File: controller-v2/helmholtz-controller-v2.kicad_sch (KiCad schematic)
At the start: 35 parts, among them J1 Screw_Terminal_01x02, J2 Screw_Terminal_01x02, J3 Screw_Terminal_01x02, J4 Screw_Terminal_01x02, U1 BDS63150AFM, U2 BDS63150AFM, U3 INA226, U4 INA226, U5 BDS63150AFM, U6 INA226, U7 RPi_Pico

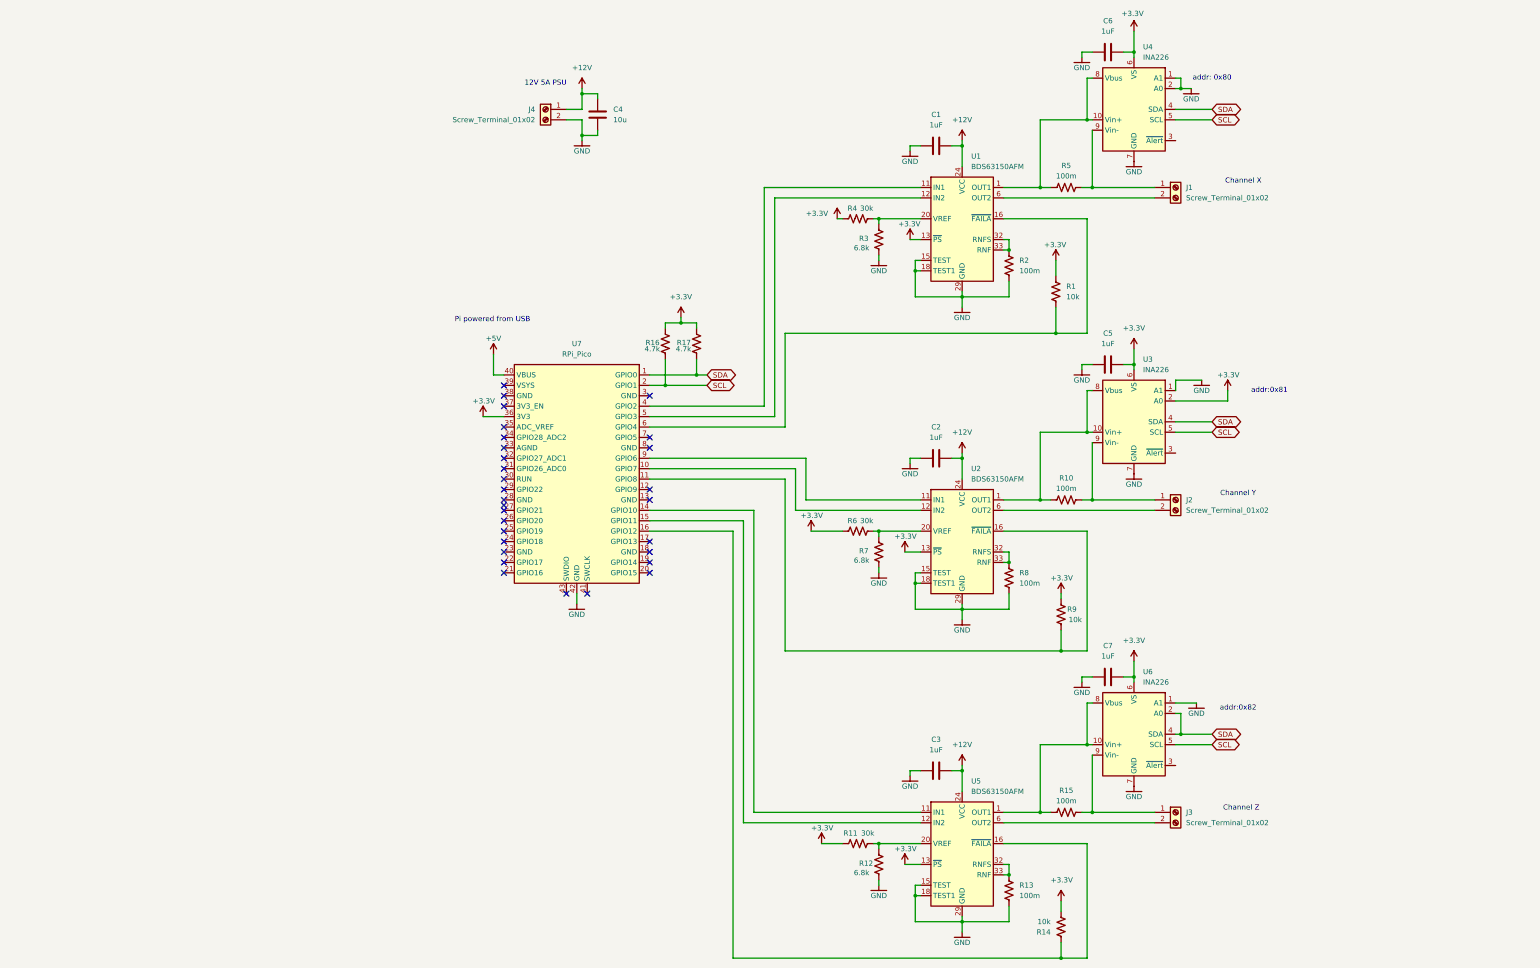
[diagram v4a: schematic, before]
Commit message: Indicators & test points added
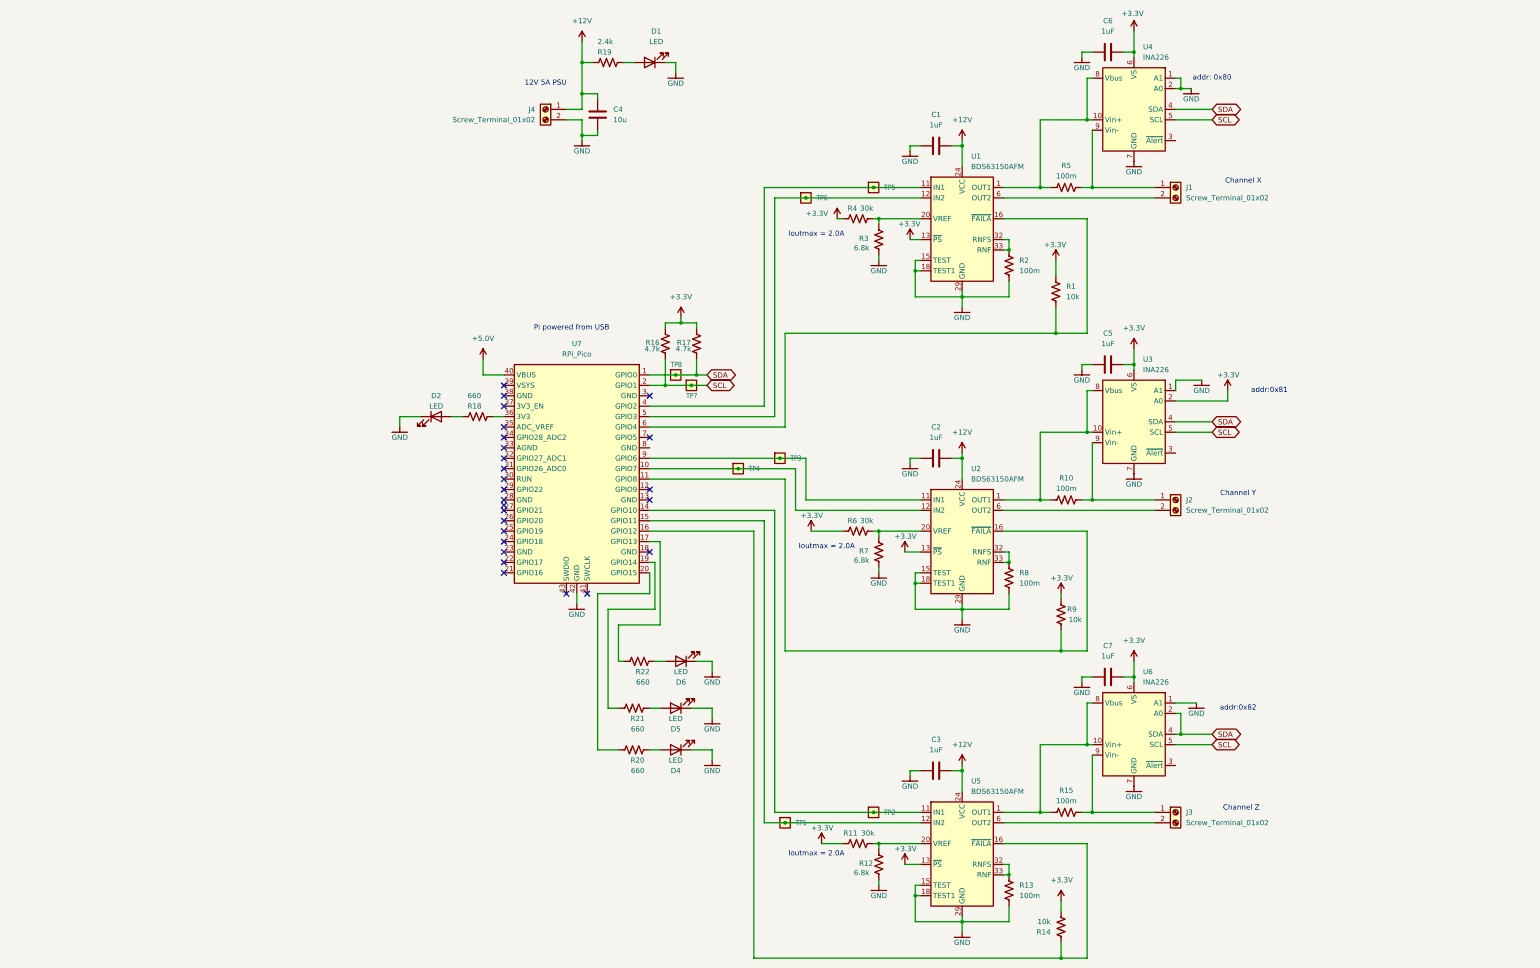
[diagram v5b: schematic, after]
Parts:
- added D1, D2, D4, D5, D6: LED, LED_SMD:LED_0603_1608Metric, symbol Device:LED
- added R18, R20, R21, R22: 660, Resistor_SMD:R_0603_1608Metric, symbol Device:R_US
- added R19: 2.4k, Resistor_SMD:R_0603_1608Metric, symbol Device:R_US
- added TP1, TP2, TP3, TP4, TP5, TP6, TP7, TP8: Test-Point, oresat-misc:TestPoint-0.75mm-th, symbol oresat-misc:Test-Point-0.75mm-th
- U7: footprint oresat-misc:RPi_Pico_TH -> oresat-misc:RPi_Pico_Castellated
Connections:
- net +12V: now also R19.1
- net +3.3V: no longer U7.36 (3V3)
- net GND: now also D1.1 (K), D2.1 (K), D4.1 (K), D5.1 (K), D6.1 (K)
- net SCL: now also TP7.1
- net SDA: now also TP8.1
- net at U2.12 (IN2), U7.10 (GPIO7): now also TP4.1
- net at U5.11 (IN1), U7.14 (GPIO10): now also TP2.1
- net at U5.12 (IN2), U7.15 (GPIO11): now also TP1.1
- net at U7.17 (GPIO13): now also R22.2
- net at U7.19 (GPIO14): now also R21.2
- net at U7.20 (GPIO15): now also R20.2
- net at U1.11 (IN1), U7.4 (GPIO2): now also TP5.1
- net at U1.12 (IN2), U7.5 (GPIO3): now also TP6.1
- net at U2.11 (IN1), U7.9 (GPIO6): now also TP3.1
- net +5V renamed +5.0V
- new net: R18.2, U7.36 (3V3)
- new net: D4.2 (A), R20.1
- new net: D5.2 (A), R21.1
- new net: D1.2 (A), R19.2
- new net: D6.2 (A), R22.1
- new net: D2.2 (A), R18.1
- no-connect marks 30 -> 26
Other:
- note added: "Ioutmax = 2.0A"

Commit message: Pre-final review
UART still needs to be connected
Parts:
- added J5: Conn_01x04, Connector_PinHeader_2.54mm:PinHeader_1x04_P2.54mm_Vertical, symbol Connector_Generic:Conn_01x04
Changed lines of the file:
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@@
+	)
+	(symbol
+		(lib_id "Connector_Generic:Conn_01x04")
+		(at 86.36 137.16 180)
+		(unit 1)
+		(exclude_from_sim no)
+		(in_bom yes)
+		(on_board yes)
+		(dnp no)
+		(fields_autoplaced yes)
+		(property "Reference" "J5"
+			(at 86.36 125.73 0)
+			(effects
+				(font
+					(size 1.27 1.27)
+				)
+			)
+		)
+		(property "Value" "Conn_01x04"
+			(at 86.36 128.27 0)
+			(effects
+				(font
+					(size 1.27 1.27)
+				)
+			)
+		)
+		(property "Footprint" "Connector_PinHeader_2.54mm:PinHeader_1x04_P2.54mm_Vertical"
+			(at 86.36 137.16 0)
+			(effects
+				(font
+					(size 1.27 1.27)
+				)
+				(hide yes)
+			)
+		)
+		(property "Datasheet" "~"
+			(at 86.36 137.16 0)
+			(effects
+				(font
+					(size 1.27 1.27)
+				)
+				(hide yes)
+			)
+		)
+		(property "Description" "Generic connector, single row, 01x04, script generated (kicad-library-utils/schlib/autogen/connector/)"
+			(at 86.36 137.16 0)
+			(effects
+				(font
+					(size 1.27 1.27)
+				)
+				(hide yes)
+			)
+		)
+		(pin "4"
+		)
+		(pin "1"
+		)
+		(pin "3"
+		)
+		(pin "2"
+		)
+		(instances
+			(project ""
+				(path "/bfab2723-d56a-4a67-8e95-4340e733d062"
+					(reference "J5")
+					(unit 1)
+				)
+			)
+		)
 	)
 	(symbol

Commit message: Pre-final Review
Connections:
- net +3.3V: now also J5.1 (Pin_1), R18.2, U7.36 (3V3)
- net GND: now also J5.4 (Pin_4), U7.13 (GND), U7.18 (GND), U7.28 (GND), U7.3 (GND), U7.33 (AGND), U7.38 (GND), U7.8 (GND)
- net at U7.21 (GPIO16): now also J5.3 (Pin_3)
- net at U7.22 (GPIO17): now also J5.2 (Pin_2)
- no-connect marks 26 -> 17
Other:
- note added: "PICO-GPIO17-RX PICO-GPIO16-TX"
- moved on the sheet: D2, J5, R18

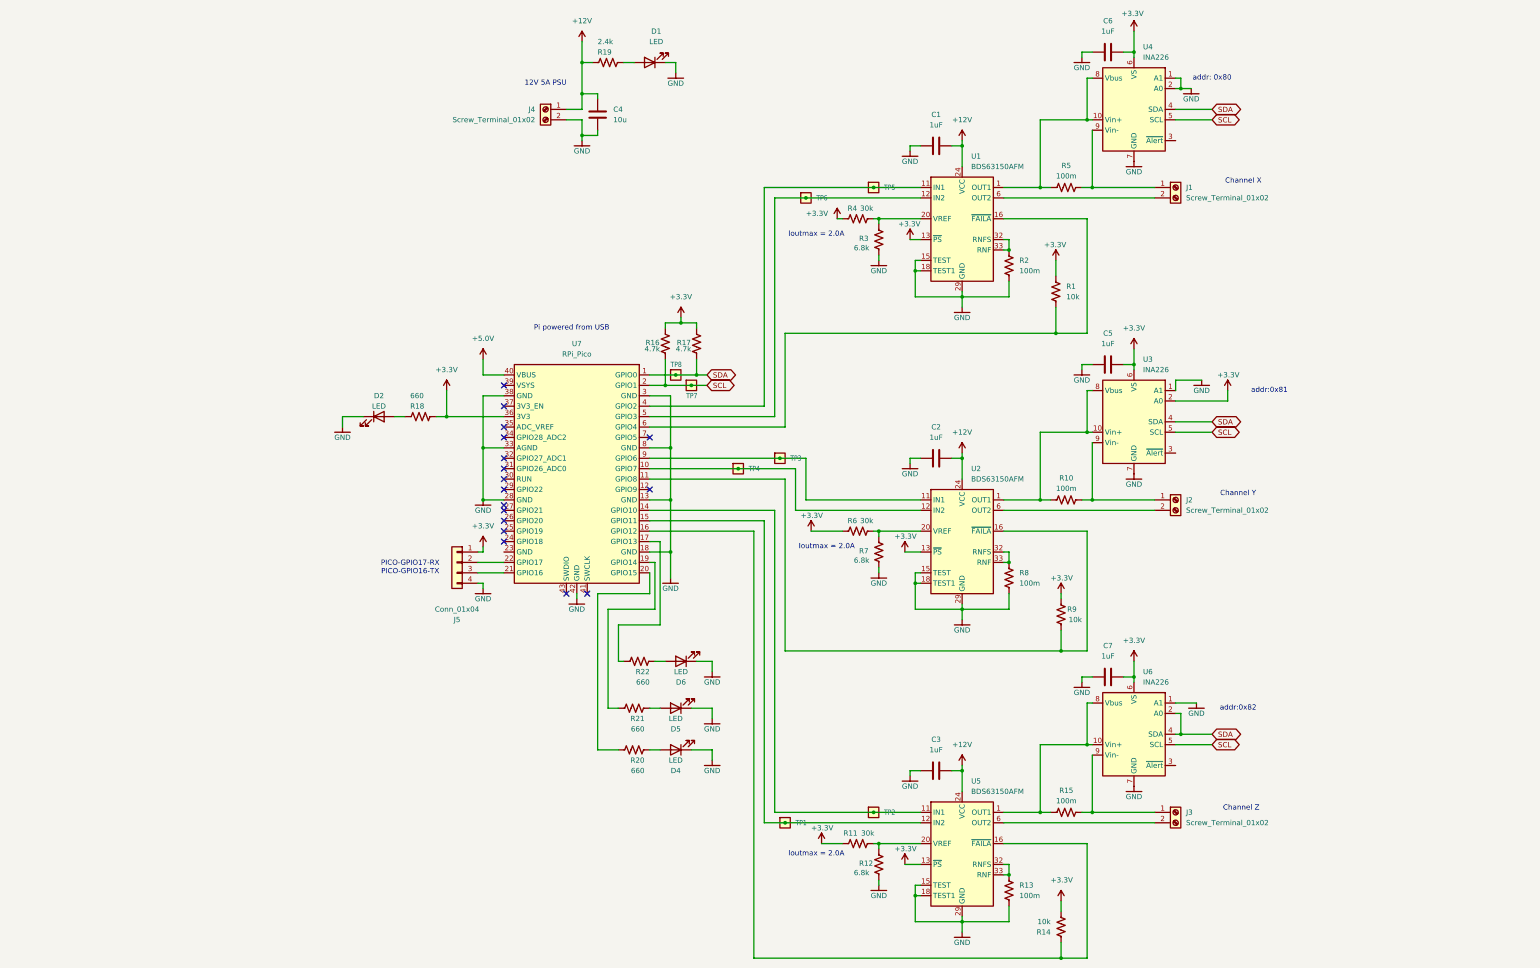
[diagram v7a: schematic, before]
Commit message: Fix BD IC symbols, fix some ERCs, put mounting holes in the schematic.
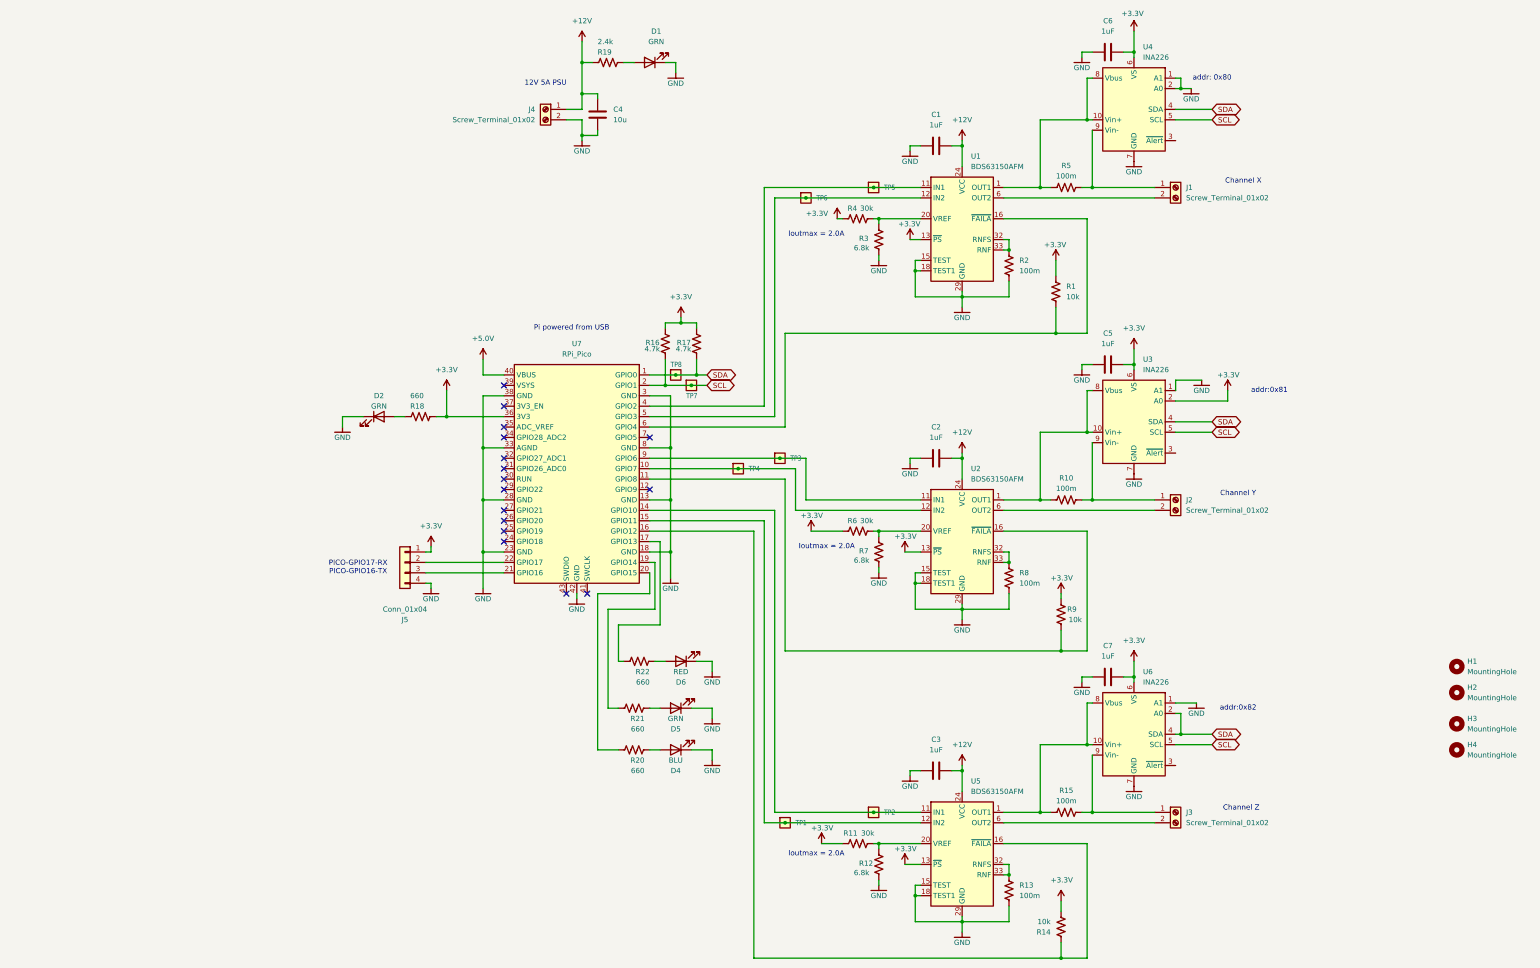
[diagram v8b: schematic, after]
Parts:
- added H1, H2, H3, H4: MountingHole, MountingHole:MountingHole_3.2mm_M3, symbol Mechanical:MountingHole
- D1, D2, D5: value LED -> GRN
- D4: value LED -> BLU
- D6: value LED -> RED
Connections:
- net GND: now also U1.22 (GND), U1.37 (GND), U1.38 (GND), U2.22 (GND), U2.37 (GND), U2.38 (GND), U5.22 (GND), U5.37 (GND), U5.38 (GND), U7.23 (GND); no longer U1.FIN, U2.FIN, U5.FIN
- no-connect marks 17 -> 16
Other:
- moved on the sheet: J5
